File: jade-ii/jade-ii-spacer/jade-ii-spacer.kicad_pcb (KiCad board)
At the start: 2 copper layers, 93 x 127.3 mm, 0 parts

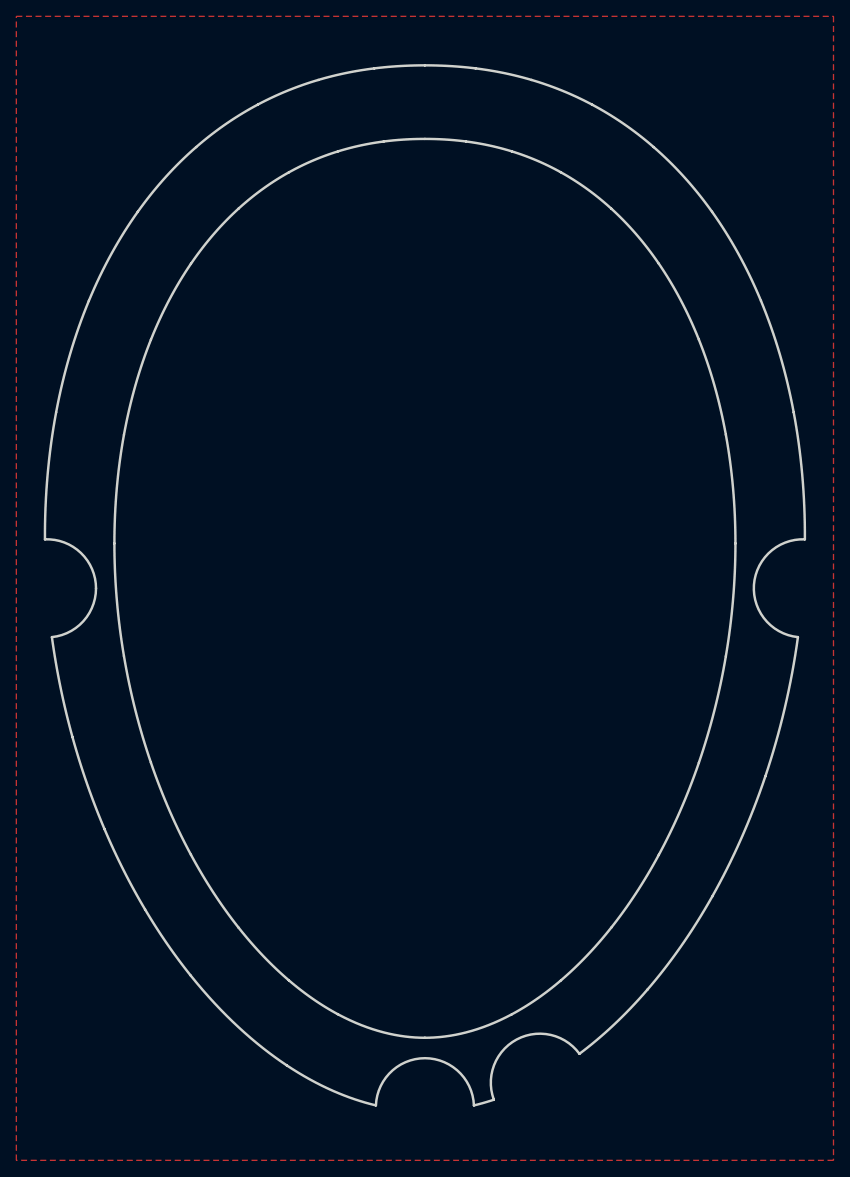
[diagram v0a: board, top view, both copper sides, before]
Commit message: jade: add mounting holes to spacer
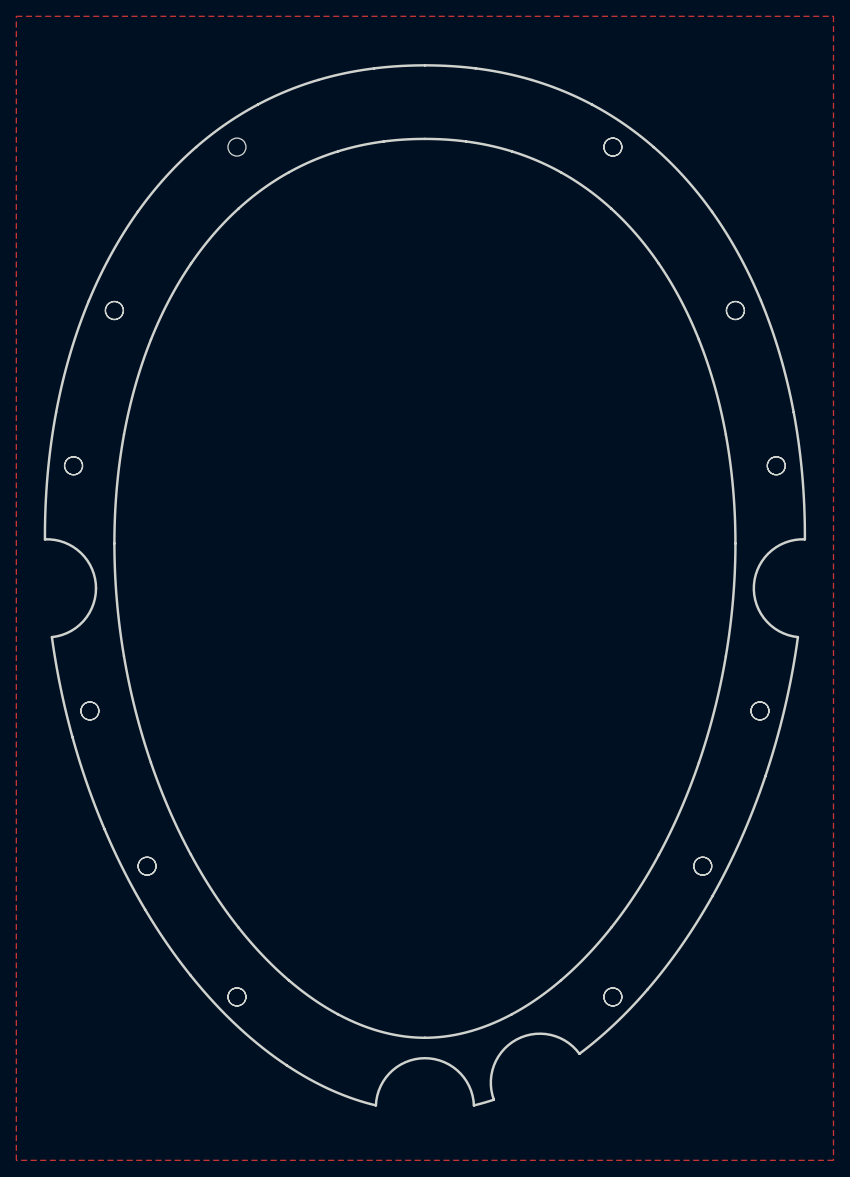
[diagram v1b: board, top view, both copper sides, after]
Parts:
- added ?: , , F.Cu at (-34.0, 34.0)
- added ?: , , F.Cu at (23.0, -54.0)
- added ?: , , F.Cu at (23.0, 50.0)
- added ?: , , F.Cu at (38.0, -34.0)
- added ?: , , F.Cu at (43.0, -15.0)
- added ?: , , F.Cu at (-23.0, 50.0)
- added ?: , , F.Cu at (-43.0, -15.0)
- added ?: , , F.Cu at (-41.0, 15.0)
- added ?: , , F.Cu at (41.0, 15.0)
- added ?: , , F.Cu at (-38.0, -34.0)
- added ?: , , F.Cu at (34.0, 34.0)
- added REF**: MountingHole_2.2mm_M2, MountingHole:MountingHole_2.2mm_M2, F.Cu at (34.0, 34.0)
- added REF**: MountingHole_2.2mm_M2, MountingHole:MountingHole_2.2mm_M2, F.Cu at (-41.0, 15.0)
- added REF**: MountingHole_2.2mm_M2, MountingHole:MountingHole_2.2mm_M2, F.Cu at (-23.0, 50.0)
- added REF**: MountingHole_2.2mm_M2, MountingHole:MountingHole_2.2mm_M2, F.Cu at (-43.0, -15.0)
- added REF**: MountingHole_2.2mm_M2, MountingHole:MountingHole_2.2mm_M2, F.Cu at (-23.0, -54.0)
- added REF**: MountingHole_2.2mm_M2, MountingHole:MountingHole_2.2mm_M2, F.Cu at (43.0, -15.0)
- added REF**: MountingHole_2.2mm_M2, MountingHole:MountingHole_2.2mm_M2, F.Cu at (38.0, -34.0)
- added REF**: MountingHole_2.2mm_M2, MountingHole:MountingHole_2.2mm_M2, F.Cu at (41.0, 15.0)
- added REF**: MountingHole_2.2mm_M2, MountingHole:MountingHole_2.2mm_M2, F.Cu at (23.0, -54.0)
- added REF**: MountingHole_2.2mm_M2, MountingHole:MountingHole_2.2mm_M2, F.Cu at (-38.0, -34.0)
- added REF**: MountingHole_2.2mm_M2, MountingHole:MountingHole_2.2mm_M2, F.Cu at (-34.0, 34.0)
- added REF**: MountingHole_2.2mm_M2, MountingHole:MountingHole_2.2mm_M2, F.Cu at (23.0, 50.0)
